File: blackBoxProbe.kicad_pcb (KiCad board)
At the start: 4 copper layers, 44 x 44 mm, 77 parts, among them J1 USB-ID, J2 JTAG_2X05, J3 JTAG_2X05, J4 Conn_01x04, Q1 Q_NMOS_DUAL, Q2 Q_PMOS_DUAL, U1 MCP1702-MB, U2 USBLC6-2, U3 STM32F103CBT, U4 74X2T45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

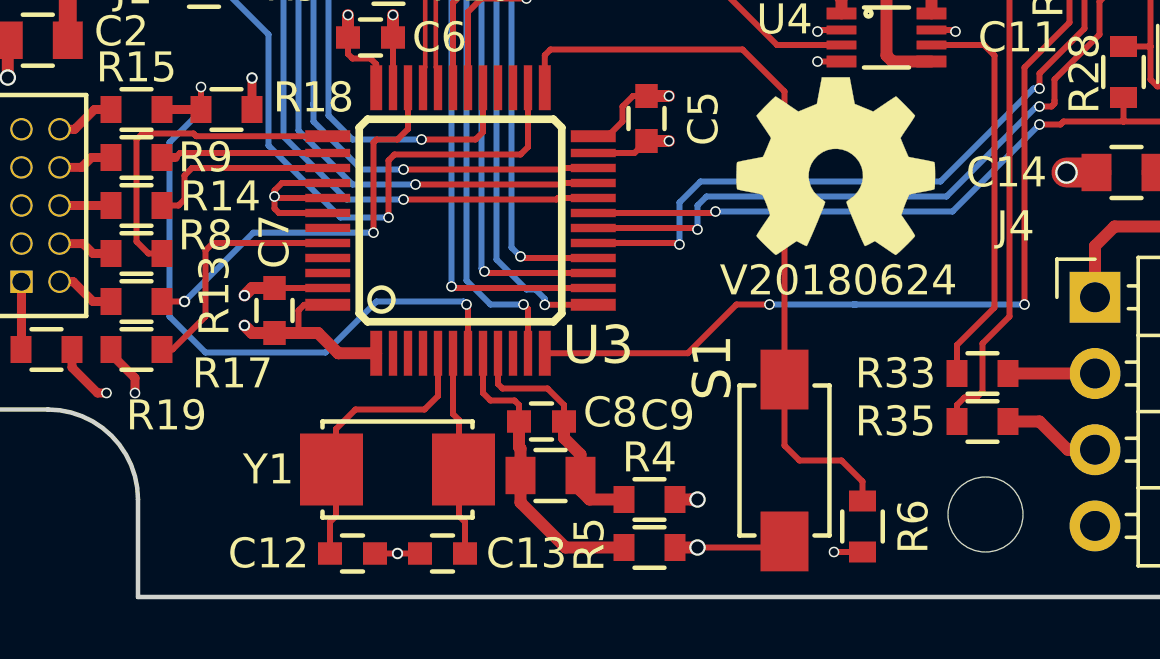
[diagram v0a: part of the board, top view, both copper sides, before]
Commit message: DONE: fixed crystal layout DONE: added a guard trace to isolate crystal from VSSA
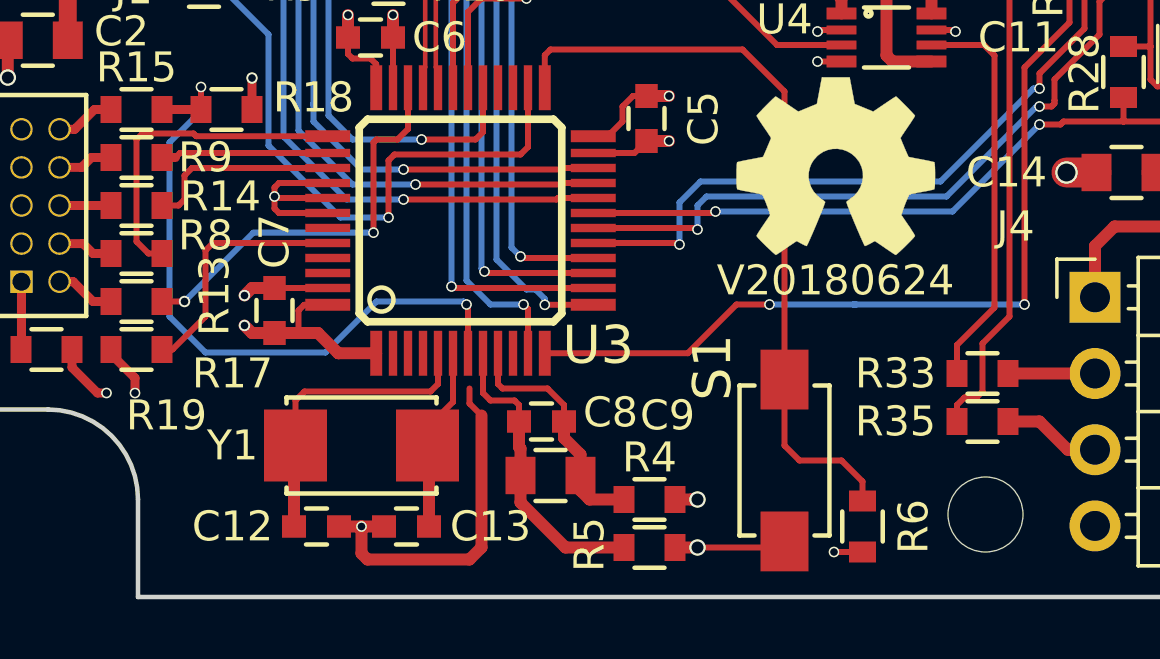
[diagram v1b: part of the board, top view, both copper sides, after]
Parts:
- moved N2 20.3 mm to (43.8, 184.7)
- moved C12 1.50 mm to (26.5, 192.9)
- moved C13 1.50 mm to (29.5, 192.9)
- moved Y1 1.44 mm to (28.0, 190.2)
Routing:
- net GND: track 68.2 -> 78.9 mm
- net Net-(C12-Pad1): track 9.51 -> 10.2 mm
- net Net-(C13-Pad1): track 6.84 -> 6.15 mm
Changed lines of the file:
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@@
     (links 181)
     (no_connects 1)
-    (area 14.224999 151.174999 58.375001 195.325001)
+    (area 3.106334 144.898 63.202 198.658666)
     (thickness 1.6)
     (drawings 10)
-    (tracks 744)
+    (tracks 750)
     (zones 0)
     (modules 77)
@@
   (layers
     (0 F.Cu signal)
-    (1 In1.Cu signal)
-    (2 In2.Cu signal)
+    (1 In1.Cu signal hide)
+    (2 In2.Cu signal hide)
     (31 B.Cu signal)
     (32 B.Adhes user)
@@
     (visible_elements FFFFFF7F)
     (pcbplotparams
-      (layerselection 0x00030_80000001)
+      (layerselection 0x010f0_80000007)
       (usegerberextensions false)
-      (excludeedgelayer true)
-      (linewidth 0.100000)
+      (usegerberattributes true)
+      (excludeedgelayer false)
+      (linewidth 0.150000)
       (plotframeref false)
       (viasonmask false)
       (mode 1)
-      (useauxorigin false)
+      (useauxorigin true)
       (hpglpennumber 1)
       (hpglpenspeed 20)
@@
       (outputformat 1)
       (mirror false)
-      (drillshape 1)
+      (drillshape 0)
       (scaleselection 1)
-      (outputdirectory ""))
+      (outputdirectory plots/))
   )
   (net 0 "")
@@
     (add_net VDDA)
   )
+  (module SquantorCrystal:X_5.0_3.2 (layer F.Cu)
+    (at 28 190.2)
+    (fp_text reference Y1 (at -4.3 0) (layer F.SilkS)
+      (effects (font (size 1 1) (thickness 0.15)))
+    )
+    (fp_text value 8.000MHz (at 0 2.5) (layer F.Fab)
+      (effects (font (size 1 1) (thickness 0.15)))
+    )
+    (fp_line (start -2.5 1.6) (end -2.5 1.4) (layer F.SilkS) (width 0.15))
+    (fp_line (start 2.5 1.6) (end 2.5 1.4) (layer F.SilkS) (width 0.15))
+    (fp_line (start 2.5 -1.6) (end 2.5 -1.4) (layer F.SilkS) (width 0.15))
+    (fp_line (start -2.5 -1.6) (end -2.5 -1.4) (layer F.SilkS) (width 0.15))
+    (fp_line (start -2.5 1.6) (end 2.5 1.6) (layer F.SilkS) (width 0.15))
+    (fp_line (start -2.5 -1.6) (end 2.5 -1.6) (layer F.SilkS) (width 0.15))
+    (pad 1 smd rect (at -2.2 0) (size 2.1 2.4) (layers F.Cu F.Paste F.Mask)
+      (net 8 "Net-(C12-Pad1)"))
+    (pad 2 smd rect (at 2.2 0) (size 2.1 2.4) (layers F.Cu F.Paste F.Mask)
+      (net 9 "Net-(C13-Pad1)"))
+  )
   (module SquantorRcl:R_0603_hand (layer F.Cu)
     (at 28.5 154.2 180)
@@
   )
   (module SquantorLabels:Label_version (layer F.Cu)
-    (at 25.57 193.55)
+    (at 43.8 184.7)
     (fp_text reference N2 (at 0 2) (layer F.Fab) hide
       (effects (font (size 1 1) (thickness 0.15)))
     )
-    (fp_text value V20180624 (at 18.33 -8.85) (layer F.SilkS)
+    (fp_text value V20180624 (at 0 0) (layer F.SilkS)
       (effects (font (size 1 1) (thickness 0.15)))
     )
@@
   )
   (module SquantorRcl:C_0603 (layer F.Cu)
-    (at 27.7 193.8)
+    (at 26.5 192.9)
     (descr "Capacitor SMD 0603, reflow soldering, AVX (see smccp.pdf)")
     (tags "capacitor 0603")
@@
   )
   (module SquantorRcl:C_0603 (layer F.Cu)
-    (at 30.7 193.8 180)
+    (at 29.5 192.9 180)
     (descr "Capacitor SMD 0603, reflow soldering, AVX (see smccp.pdf)")
     (tags "capacitor 0603")
@@
     )
   )
-  (module SquantorCrystal:X_5.0_3.2 (layer F.Cu)
-    (at 29.2 191)
-    (fp_text reference Y1 (at -4.3 0) (layer F.SilkS)
-      (effects (font (size 1 1) (thickness 0.15)))
-    )
-    (fp_text value 8.000MHz (at 0 2.5) (layer F.Fab)
-      (effects (font (size 1 1) (thickness 0.15)))
-    )
-    (fp_line (start -2.5 1.6) (end -2.5 1.4) (layer F.SilkS) (width 0.15))
-    (fp_line (start 2.5 1.6) (end 2.5 1.4) (layer F.SilkS) (width 0.15))
-    (fp_line (start 2.5 -1.6) (end 2.5 -1.4) (layer F.SilkS) (width 0.15))
-    (fp_line (start -2.5 -1.6) (end -2.5 -1.4) (layer F.SilkS) (width 0.15))
-    (fp_line (start -2.5 1.6) (end 2.5 1.6) (layer F.SilkS) (width 0.15))
-    (fp_line (start -2.5 -1.6) (end 2.5 -1.6) (layer F.SilkS) (width 0.15))
-    (pad 1 smd rect (at -2.2 0) (size 2.1 2.4) (layers F.Cu F.Paste F.Mask)
-      (net 8 "Net-(C12-Pad1)"))
-    (pad 2 smd rect (at 2.2 0) (size 2.1 2.4) (layers F.Cu F.Paste F.Mask)
-      (net 9 "Net-(C13-Pad1)"))
-  )
   (gr_arc (start 17.55 192) (end 17.55 189) (angle 90) (layer Edge.Cuts) (width 0.15))
   (gr_arc (start 55.05 154.5) (end 55.05 157.5) (angle 90) (layer Edge.Cuts) (width 0.15))
@@
   (segment (start 21.1 166.45) (end 21.1 165.55) (width 0.6) (layer F.Cu) (net 1))
   (segment (start 21.1 166.45) (end 22.7 166.45) (width 0.6) (layer F.Cu) (net 1))
+  (segment (start 31.6 188.8) (end 31.6 188.3) (width 0.2) (layer F.Cu) (net 2))
+  (segment (start 32 189.2) (end 31.6 188.8) (width 0.2) (layer F.Cu) (net 2))
+  (segment (start 32 193.6) (end 32 189.2) (width 0.4) (layer F.Cu) (net 2))
+  (segment (start 31.6 194) (end 32 193.6) (width 0.4) (layer F.Cu) (net 2))
+  (segment (start 28.2 194) (end 31.6 194) (width 0.4) (layer F.Cu) (net 2))
+  (segment (start 28 193.8) (end 28.2 194) (width 0.4) (layer F.Cu) (net 2))
+  (segment (start 28 192.9) (end 28 193.8) (width 0.4) (layer F.Cu) (net 2))
+  (segment (start 28.75 192.9) (end 28 192.9) (width 0.4) (layer F.Cu) (net 2))
+  (segment (start 27.25 192.9) (end 28 192.9) (width 0.4) (layer F.Cu) (net 2))
+  (via (at 28 192.9) (size 0.3556) (drill 0.254) (layers F.Cu B.Cu) (net 2))
   (segment (start 24.3 168.7) (end 24.5 168.9) (width 0.2) (layer F.Cu) (net 2))
   (via (at 24.5 168.9) (size 0.3556) (drill 0.254) (layers F.Cu B.Cu) (net 2))
@@
   (segment (start 23.25 170.65) (end 23.6 171) (width 0.4) (layer F.Cu) (net 2))
   (segment (start 22.3 170.65) (end 23.25 170.65) (width 0.4) (layer F.Cu) (net 2))
-  (segment (start 29.95 193.8) (end 29.2 193.8) (width 0.2) (layer F.Cu) (net 2))
-  (via (at 29.2 193.8) (size 0.381) (drill 0.254) (layers F.Cu B.Cu) (net 2))
-  (segment (start 28.45 193.8) (end 29.2 193.8) (width 0.2) (layer F.Cu) (net 2))
   (segment (start 29.05 178.275) (end 29.05 176.6) (width 0.2) (layer F.Cu) (net 2))
   (via (at 24.1 185.2) (size 0.381) (drill 0.254) (layers F.Cu B.Cu) (net 2))
@@
   (segment (start 18.225 174.545) (end 18.975 174.545) (width 0.6) (layer F.Cu) (net 3))
   (segment (start 18.21 176.69) (end 18.21 174.56) (width 0.6) (layer F.Cu) (net 3))
+  (segment (start 25.1 181.9) (end 25.1 181.6) (width 0.2) (layer F.Cu) (net 4))
+  (segment (start 25.1 181.6) (end 25.25 181.45) (width 0.2) (layer F.Cu) (net 4))
+  (segment (start 25.25 181.45) (end 25.35 181.45) (width 0.2) (layer F.Cu) (net 4))
+  (segment (start 25.35 181.45) (end 26.875 181.45) (width 0.2) (layer F.Cu) (net 4))
   (segment (start 27.65 152.6) (end 26.4 152.6) (width 0.4) (layer F.Cu) (net 4))
   (segment (start 26.4 152.6) (end 26 153) (width 0.4) (layer F.Cu) (net 4))
@@
   (via (at 25.1 181.9) (size 0.3556) (drill 0.254) (layers F.Cu B.Cu) (net 4))
   (segment (start 25.1 182) (end 25.1 181.9) (width 0.2) (layer F.Cu) (net 4))
-  (segment (start 25.1 181.9) (end 25.1 181.7) (width 0.2) (layer F.Cu) (net 4))
   (segment (start 26.875 181.95) (end 25.15 181.95) (width 0.2) (layer F.Cu) (net 4))
   (segment (start 25.15 181.95) (end 25.1 181.9) (width 0.2) (layer F.Cu) (net 4))
-  (segment (start 25.1 181.7) (end 25.35 181.45) (width 0.2) (layer F.Cu) (net 4))
-  (segment (start 25.35 181.45) (end 26.875 181.45) (width 0.2) (layer F.Cu) (net 4))
   (segment (start 25.25 182.45) (end 25.1 182.3) (width 0.2) (layer F.Cu) (net 4))
   (segment (start 26.875 182.45) (end 25.25 182.45) (width 0.2) (layer F.Cu) (net 4))
@@
   (segment (start 54.75 172) (end 54.75 172.85) (width 0.2) (layer F.Cu) (net 7))
   (segment (start 54.75 170.4) (end 54.75 172) (width 0.2) (layer F.Cu) (net 7))
-  (segment (start 30.1 189) (end 30.55 188.55) (width 0.2) (layer F.Cu) (net 8))
-  (segment (start 30.55 188.55) (end 30.55 187.125) (width 0.2) (layer F.Cu) (net 8))
-  (segment (start 27.8 189) (end 30.1 189) (width 0.2) (layer F.Cu) (net 8))
-  (segment (start 27.15022 189.64978) (end 27.8 189) (width 0.2) (layer F.Cu) (net 8))
-  (segment (start 27.15022 191) (end 27.15022 189.64978) (width 0.2) (layer F.Cu) (net 8))
-  (segment (start 26.95 192.75) (end 27.15022 192.54978) (width 0.2) (layer F.Cu) (net 8))
-  (segment (start 27.15022 192.54978) (end 27.15022 191) (width 0.2) (layer F.Cu) (net 8))
-  (segment (start 26.95 193.8) (end 26.95 192.75) (width 0.2) (layer F.Cu) (net 8))
-  (segment (start 31.24978 189.34978) (end 31.05 189.15) (width 0.2) (layer F.Cu) (net 9))
-  (segment (start 31.05 189.15) (end 31.05 187.125) (width 0.2) (layer F.Cu) (net 9))
-  (segment (start 31.24978 191) (end 31.24978 189.34978) (width 0.2) (layer F.Cu) (net 9))
-  (segment (start 31.45 192.75) (end 31.24978 192.54978) (width 0.2) (layer F.Cu) (net 9))
-  (segment (start 31.24978 192.54978) (end 31.24978 191) (width 0.2) (layer F.Cu) (net 9))
-  (segment (start 31.45 193.8) (end 31.45 192.75) (width 0.2) (layer F.Cu) (net 9))
+  (segment (start 25.8 190.2) (end 25.8 188.7) (width 0.2) (layer F.Cu) (net 8))
+  (segment (start 25.8 188.7) (end 26.1 188.4) (width 0.2) (layer F.Cu) (net 8))
+  (segment (start 26.1 188.4) (end 30.3 188.4) (width 0.2) (layer F.Cu) (net 8))
+  (segment (start 30.3 188.4) (end 30.55 188.15) (width 0.2) (layer F.Cu) (net 8))
+  (segment (start 30.55 188.15) (end 30.55 187.125) (width 0.2) (layer F.Cu) (net 8))
+  (segment (start 25.75 192.9) (end 25.75 190.25) (width 0.4) (layer F.Cu) (net 8))
+  (segment (start 25.75 190.25) (end 25.8 190.2) (width 0.4) (layer F.Cu) (net 8))
+  (segment (start 30.2 189.6) (end 31.05 188.75) (width 0.2) (layer F.Cu) (net 9))
+  (segment (start 31.05 188.75) (end 31.05 187.125) (width 0.2) (layer F.Cu) (net 9))
+  (segment (start 30.2 190.2) (end 30.2 189.6) (width 0.2) (layer F.Cu) (net 9))
+  (segment (start 30.25 192.9) (end 30.25 190.25) (width 0.4) (layer F.Cu) (net 9))
+  (segment (start 30.25 190.25) (end 30.2 190.2) (width 0.4) (layer F.Cu) (net 9))
   (segment (start 47.85 158.45) (end 47.7 158.3) (width 0.4) (layer F.Cu) (net 10))
   (segment (start 47.7 158.3) (end 47.5 158.3) (width 0.4) (layer F.Cu) (net 10))

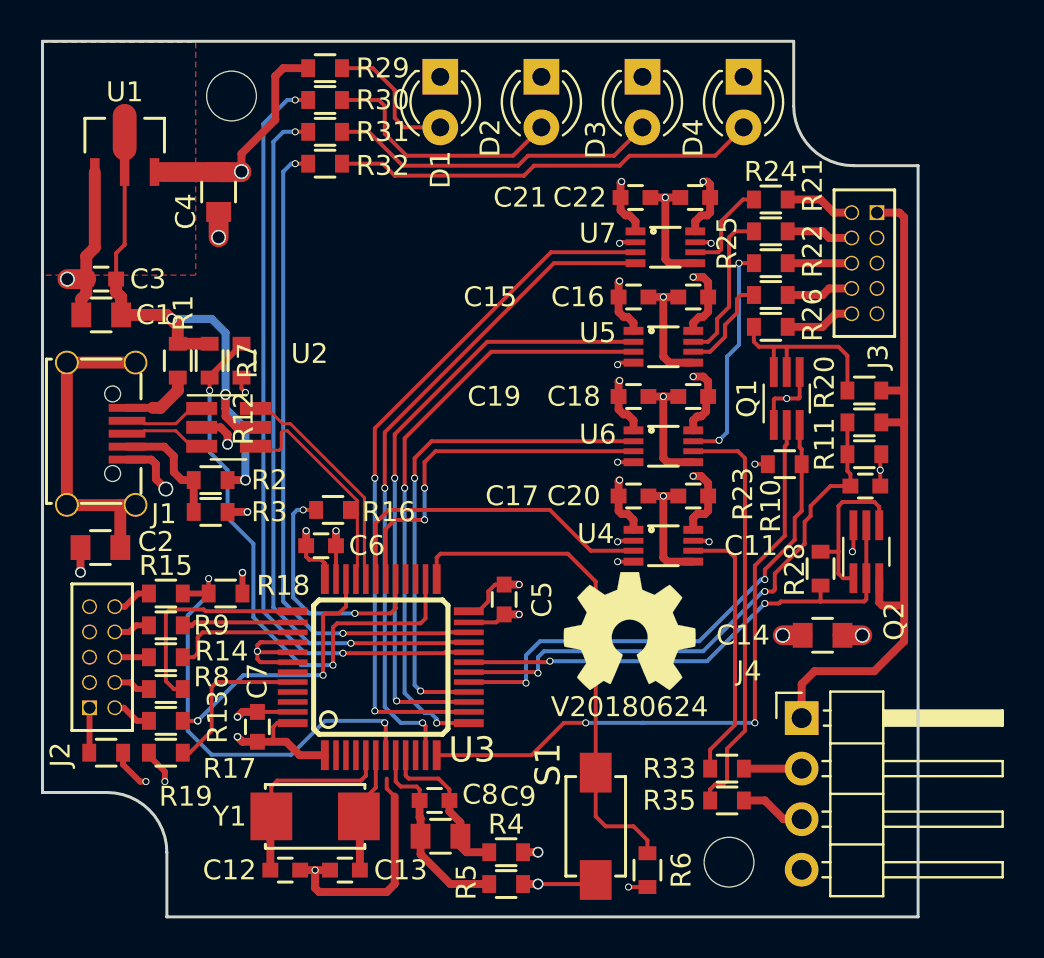
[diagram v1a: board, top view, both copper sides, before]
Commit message: FIX: incorrect naming of 74X2T45 gate FIX: missing USB series resistors FIX: added another label for the project name
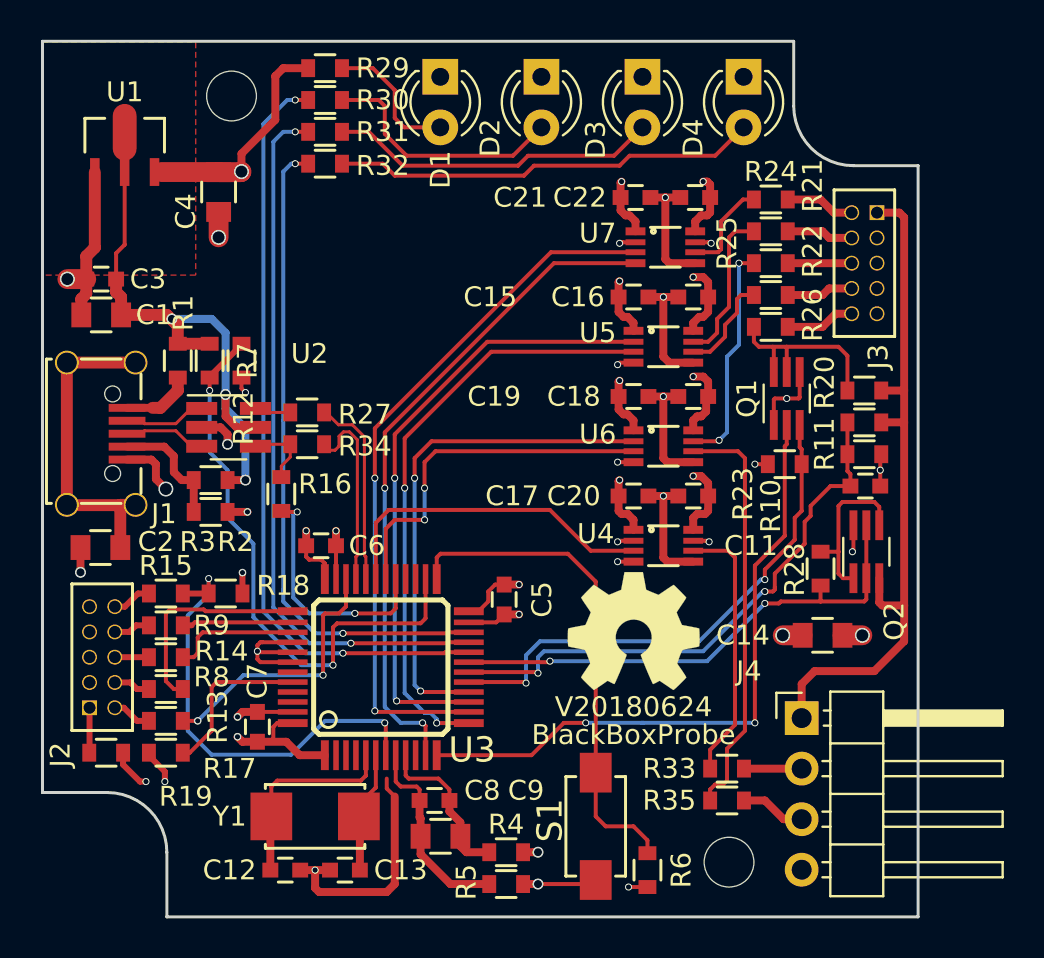
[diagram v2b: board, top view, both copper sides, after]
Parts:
- added N3: BlackBoxProbe, SquantorLabels:Label_version, F.Cu at (36.3, 205.3)
- added R27: 22, SquantorRcl:R_0603_hand, F.Cu at (27.6, 169.9)
- added R34: 22, SquantorRcl:R_0603_hand, F.Cu at (27.6, 171.5)
- moved R16 2.72 mm to (26.3, 174.0), turned to 90 degrees
- moved N1 0.20 mm to (44.0, 180.9)
- moved N2 0.20 mm to (44.0, 184.7)
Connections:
- R16 pad 2: /USB_D+ -> Net-(R16-Pad2)
- U2 pad 4: /USB_D+ -> Net-(R16-Pad2)
- U2 pad 6: /USB_D- -> Net-(R27-Pad2)
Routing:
- net Net-(R16-Pad2): track 0.00 -> 3.63 mm
- net /USB_D+: track 13.1 -> 9.67 mm
- net /USB_D-: track 11.9 -> 9.71 mm
- net Net-(R27-Pad2): track 0.00 -> 1.83 mm

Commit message: DONE: rerouted everything after fixing the pinout of the header
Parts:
- J2: footprint SquantorConnectors:Header-0127-2X5-H006 -> SquantorConnectors:Header-0127-2X05-H006
- J3: footprint SquantorConnectors:Header-0127-2X5-H006 -> SquantorConnectors:Header-Shr-0127-2X05-H006
- moved R23 15.2 mm to (43.4, 159.7), turned to 270 degrees
- moved R20 10.7 mm to (50.9, 159.2)
- moved Q1 10.5 mm to (47.0, 159.8), turned to 0 degrees
- moved C17 8.68 mm to (39.0, 167.0)
- moved C20 8.68 mm to (42.0, 167.0)
- moved U4 8.68 mm to (40.5, 169.5)
- moved R18 8.54 mm to (20.5, 187.0), turned to 0 degrees
- moved R24 8.00 mm to (50.9, 167.2)
- moved C18 7.16 mm to (47.9, 162.0)
- moved C19 7.16 mm to (44.9, 162.0)
- moved U6 7.16 mm to (46.4, 164.5)
- moved Q2 6.86 mm to (50.8, 172.1), turned to 270 degrees
- moved R13 6.40 mm to (20.5, 179.0)
- moved R15 6.40 mm to (20.5, 185.4)
- moved C21 5.87 mm to (39.0, 162.0)
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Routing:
- net /PROBE_I_RST_SEN: track 26.4 -> 38.2 mm
- net /PROBE_VDD: track 74.9 -> 86.4 mm
- net /PROBE_E_TDO: track 11.4 -> 2.25 mm, vias 2 -> 0
- net /PROBE_I_TCK: track 31.0 -> 22.0 mm
- net /MCU_RST: track 22.9 -> 14.5 mm
- net /PROBE_E_RX: track 20.9 -> 28.6 mm, vias 0 -> 2
- net /PROBE_E_TX: track 13.4 -> 20.9 mm
- net /PROBE_I_TDI: track 30.1 -> 22.7 mm
- net /PROBE_I_TDO: track 25.6 -> 33.0 mm
- net Net-(J2-Pad1): track 2.27 -> 9.27 mm
- net /PROBE_I_RST: track 32.4 -> 38.7 mm
- net /PROBE_I_RX: track 18.3 -> 24.2 mm
- net /PROBE_TMS_DIR: track 33.8 -> 28.5 mm
- net /TARGET_PWR_EN: track 25.8 -> 31.0 mm
- net /PROBE_I_TMS: track 35.7 -> 30.5 mm
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
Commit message: WIP: final placement of silk, need some checks
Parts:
- moved C15 5.00 mm to (44.9, 162.0)
- moved C16 5.00 mm to (47.9, 162.0)
- moved C18 5.00 mm to (47.9, 167.0)
- moved C19 5.00 mm to (44.9, 167.0)
- moved U5 5.00 mm to (46.4, 164.5)
- moved U6 5.00 mm to (46.4, 169.5)
- moved R26 0.05 mm to (51.0, 160.8)
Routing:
- net /PROBE_I_TCK: track 22.0 -> 33.3 mm
- net /PROBE_I_TDI: track 22.7 -> 34.0 mm
- net /PROBE_E_RX: track 28.6 -> 22.0 mm, vias 2 -> 0
- net /PROBE_I_RX: track 24.2 -> 18.0 mm
- net /PROBE_E_TDI: track 10.1 -> 4.21 mm
- net /PROBE_E_TDO: track 2.25 -> 8.13 mm
- net /PROBE_I_TDO: track 33.0 -> 28.5 mm
- net /PROBE_E_TCK: track 5.83 -> 3.62 mm
- net /PROBE_I_TX: track 13.5 -> 12.8 mm
- net /PROBE_VDD: track 86.4 -> 86.9 mm
- net /PROBE_E_TMS: vias 2 -> 0
